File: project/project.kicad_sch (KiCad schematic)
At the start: 37 parts, among them J101 XT-IN, J102 IN, J103 5V, J104 OUT, Q101 HYG210P06LQ1D, U101 XL4001

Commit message: more layout
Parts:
- removed D101: LED-R, LED_SMD:LED_0805_2012Metric_Pad1.15x1.40mm_HandSolder, symbol Device:LED
- removed D103: LED-G, LED_SMD:LED_0805_2012Metric_Pad1.15x1.40mm_HandSolder, symbol Device:LED
- removed D106: GREEN, LED_SMD:LED_0805_2012Metric_Pad1.15x1.40mm_HandSolder, symbol Device:LED_Small_Filled
- added C3, C4: 220u/35v, Capacitor_SMD:CP_Elec_10x10, symbol Device:C_Polarized
- added C5: 10u/35v, Capacitor_SMD:C_1206_3216Metric, symbol Device:C
- added D1: LED-R, LED_SMD:LED_0805_2012Metric_Pad1.15x1.40mm_HandSolder, symbol Device:LED_Small_Filled
- added D3, D6: LED-G, LED_SMD:LED_0805_2012Metric_Pad1.15x1.40mm_HandSolder, symbol Device:LED_Small_Filled
- added H6: MP, MountingHole:MountingHole_3.2mm_M3_Pad_Via, symbol Mechanical:MountingHole_Pad
- U1: renamed from U101; footprint -local:Texas_HTSOP-8-1EP_3.9x4.9mm_P1.27mm_EP2.8x4.1mm_Mask2.8x4.1mm_ThermalVias -> Package_SO:Texas_HTSOP-8-1EP_3.9x4.9mm_P1.27mm_EP2.95x4.9mm_Mask2.4x3.1mm_ThermalVias; symbol -xlsemi:XL4001 -> -local:XL4001
- renumbered C101 to C1, C107 to C10, C108 to C11, C102 to C2, C103 to C6, C104 to C7, C105 to C8, C106 to C9, D102 to D2, D104 to D4, D105 to D5, F101 to F1, G101 to G1, G102 to G2, H101 to H1, H102 to H2, H103 to H3, H104 to H4, H105 to H5, J101 to J1, J102 to J2, J103 to J3, J104 to J4, L101 to L1, Q101 to Q1, R101 to R1, R102 to R2, R103 to R3, R104 to R4, R105 to R5, R106 to R6, R107 to R7, RV101 to RV1
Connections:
- net A3 is gone; now on net +5V: J2.11 (Pin_11)
- net +24V: now also C3.1, C4.1, C5.1
- net A0: no longer J4.7 (Pin_7)
- net A1: now also J4.5 (Pin_5); no longer J4.9 (Pin_9)
- net A2: now also J4.7 (Pin_7); no longer J4.11 (Pin_11)
- net GND: now also J4.9 (Pin_9), C3.2, C4.2, C5.2, D1.2 (A), D3.1 (K), D6.1 (K), H6.1; no longer J4.5 (Pin_5), R7.1
- net VOUTp: now also R7.2
- net at R1.2, R2.2: now also D1.1 (K)
- net at R5.1: now also D3.2 (A)
- new net: D6.2 (A), R7.1
- no-connect marks 0 -> 5
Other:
- note added: "module| chip1 | chip2 | chip3 -------------------- 1 | 0x88 | 0xA8 | 0xC8 2 | 0x84 | 0xA4 | 0xC4 3 | 0x82 | 0xA2 | 0xC2 4 | 0x80 | 0xA0 | 0xC0 for chain start A0=0 A1=0 A2=1"
- title: LED Dimmer 6x6 ch -> LED Dimmer 6x6
- moved on the sheet: C1, C2, D2, J1, Q1, R1, R2, R3, R4, R5, R7

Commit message: prepared for production
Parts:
- C1, C9, D2, D4, D5, Q1, RV1, U1: jlc-part-type (none) -> E
- C10, C11, C8: WE 885012108012 -> (none); jlc-part-type (none) -> E
- C2, C3, C4: WE 875075661007 -> (none); jlc-part-type (none) -> E
- C5, C6, C7: WE 885012108022 -> (none); jlc-part-type (none) -> E
- D1: lcsc# C2297 -> C84256
- F1: value 1A -> 350mA; jlc-part-type (none) -> E; lcsc# C151135 -> C2897464
- J1: jlc-part-type (none) -> E; lcsc# (none) -> C431092
- J3: jlc-part-type (none) -> -
- L1: WE 744770147 -> (none); jlc-part-type (none) -> E
- R1, R2, R3: jlc-part-type (none) -> B; lcsc# (none) -> C17414
- R4, R5: value 10K -> 10k; lcsc# C17630 -> C17414
- R6: jlc-part-type (none) -> B; lcsc# (none) -> C4310
- R7: jlc-part-type (none) -> B; lcsc# (none) -> C17673

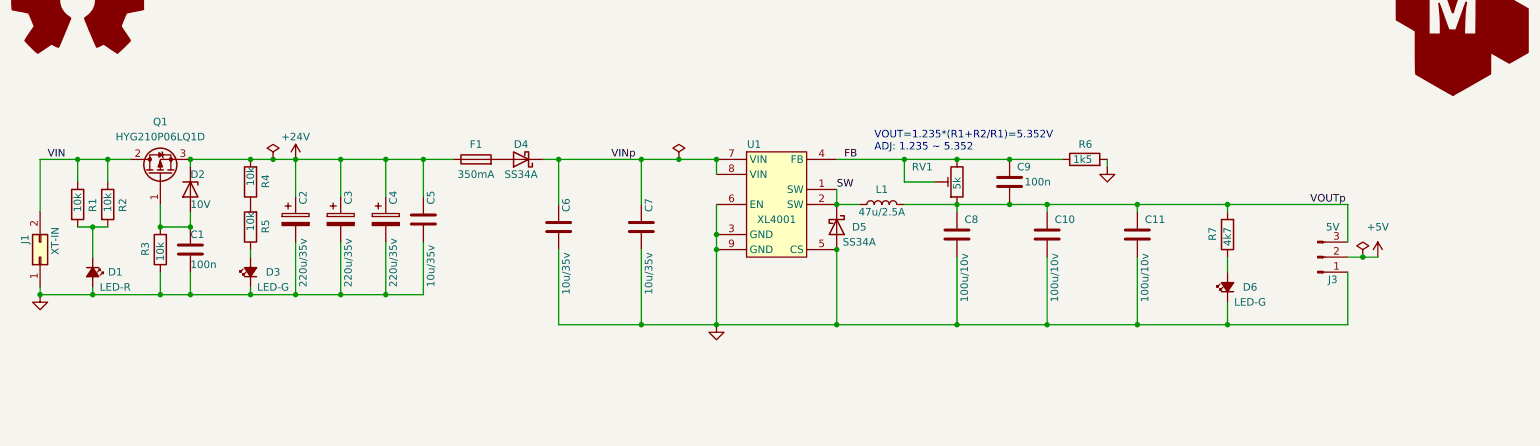
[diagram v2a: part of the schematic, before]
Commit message: improvements after first prototype test
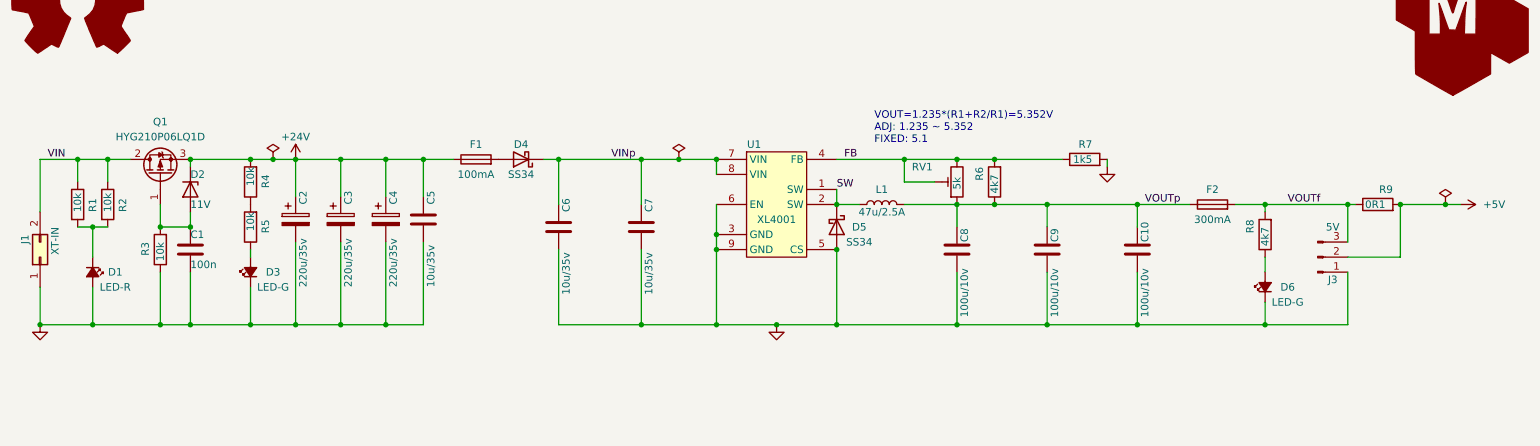
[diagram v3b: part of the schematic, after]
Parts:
- removed C9: 100n, Capacitor_SMD:C_0805_2012Metric, symbol Device:C
- added F2: 300mA, Fuse:Fuse_1206_3216Metric_Pad1.42x1.75mm_HandSolder, symbol Device:Fuse
- added R6: 4k7, Resistor_SMD:R_0805_2012Metric, symbol Device:R
- added R9: 0R1, Resistor_SMD:R_1206_3216Metric_Pad1.30x1.75mm_HandSolder, symbol Device:R
- C1: jlc-part-type E -> B; lcsc# C161260 -> C49678
- C5, C6, C7: jlc-part-type E -> B; lcsc# C92797 -> C13585
- D2: value 10V -> 11V; jlc-part-type E -> PE; lcsc# C118715 -> C22395528
- D4, D5: value SS34A -> SS34; jlc-part-type E -> B; lcsc# C2886580 -> C8678
- F1: value 350mA -> 100mA; lcsc# C2897464 -> C2830236
- renumbered C11 to C10, C10 to C9, R6 to R7, R7 to R8
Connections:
- net +5V: now also R9.2
- net FB: now also R6.2
- net VOUTp: now also F2.1, R6.1; no longer J3.3 (Pin_3), R8.2
- new net VOUTf: F2.2, J3.3 (Pin_3), R8.2, R9.1
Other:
- note added: "VOUT=1.235*(R1+R2/R1)=5.352V ADJ: 1.235 ~ 5.352 FIXED: 5.1"
- note removed: "VOUT=1.235*(R1+R2/R1)=5.352V ADJ: 1.235 ~ 5.352"
- title: LED Dimmer 6x6 -> LED_Dimmer_6x6
- moved on the sheet: C10, C8, C9, D6, R8
